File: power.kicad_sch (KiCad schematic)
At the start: 21 parts, among them J2 Conn_01x09_Pin, Q2 IRF840A, SW2 DOWNLOAD, U2 UC3843_DIP8, U7 AP2112K-3.3, U8 ESP32-S3-MINI-1

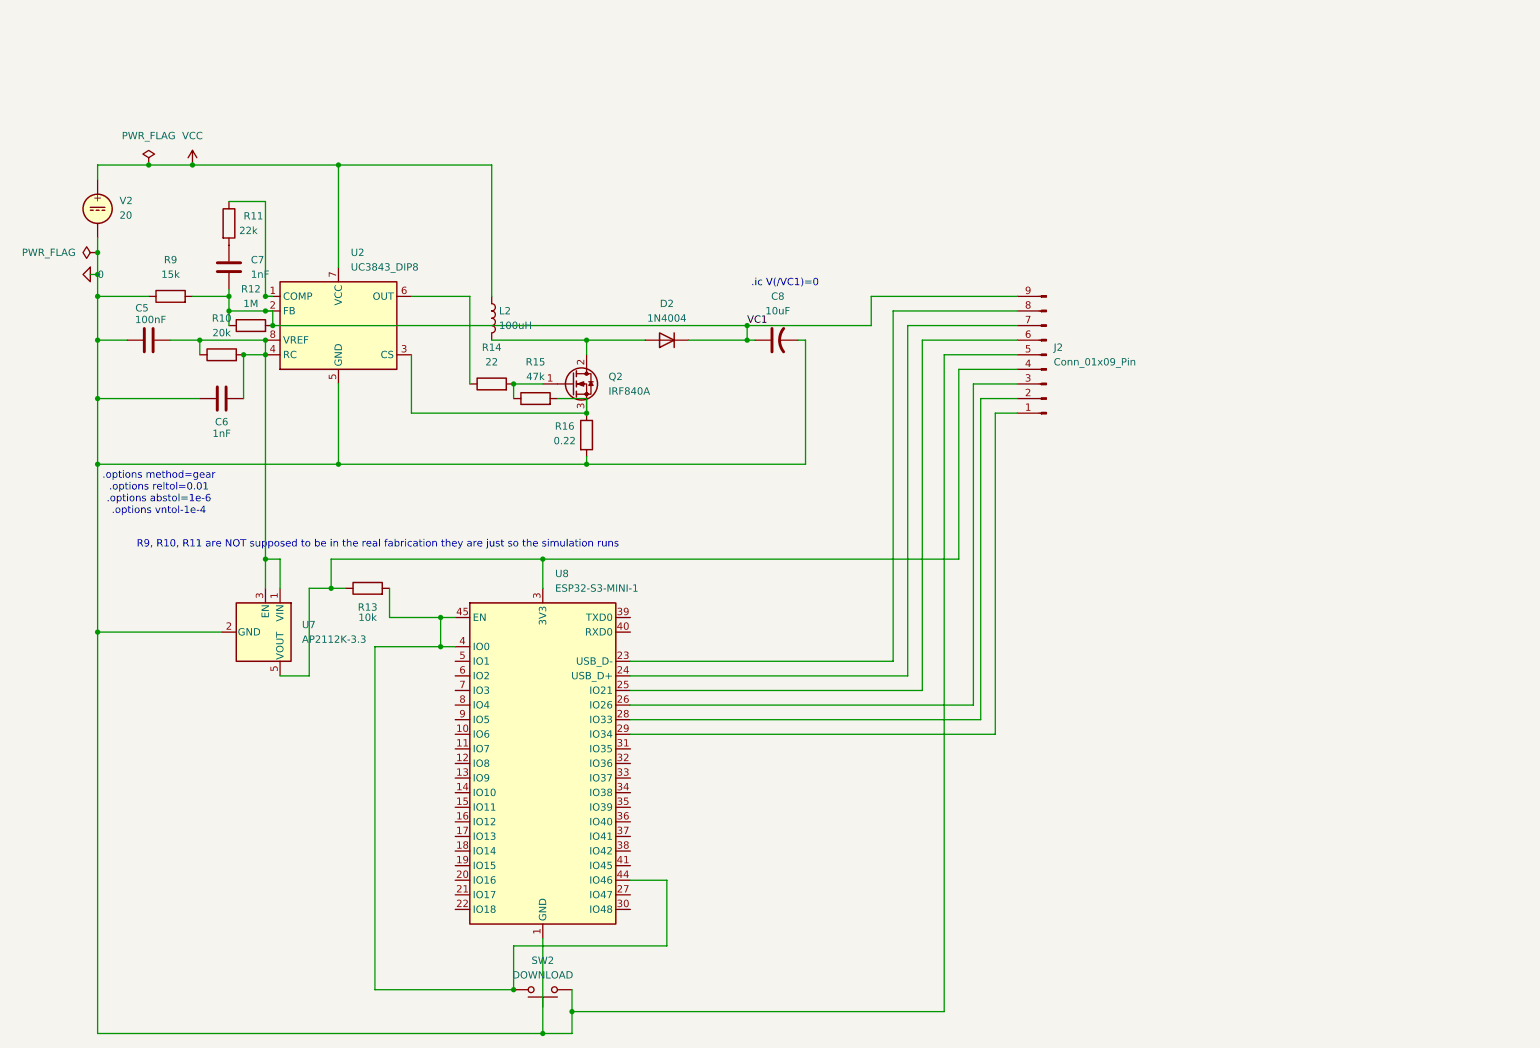
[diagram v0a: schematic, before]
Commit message: improve boost converter design and move to net labels
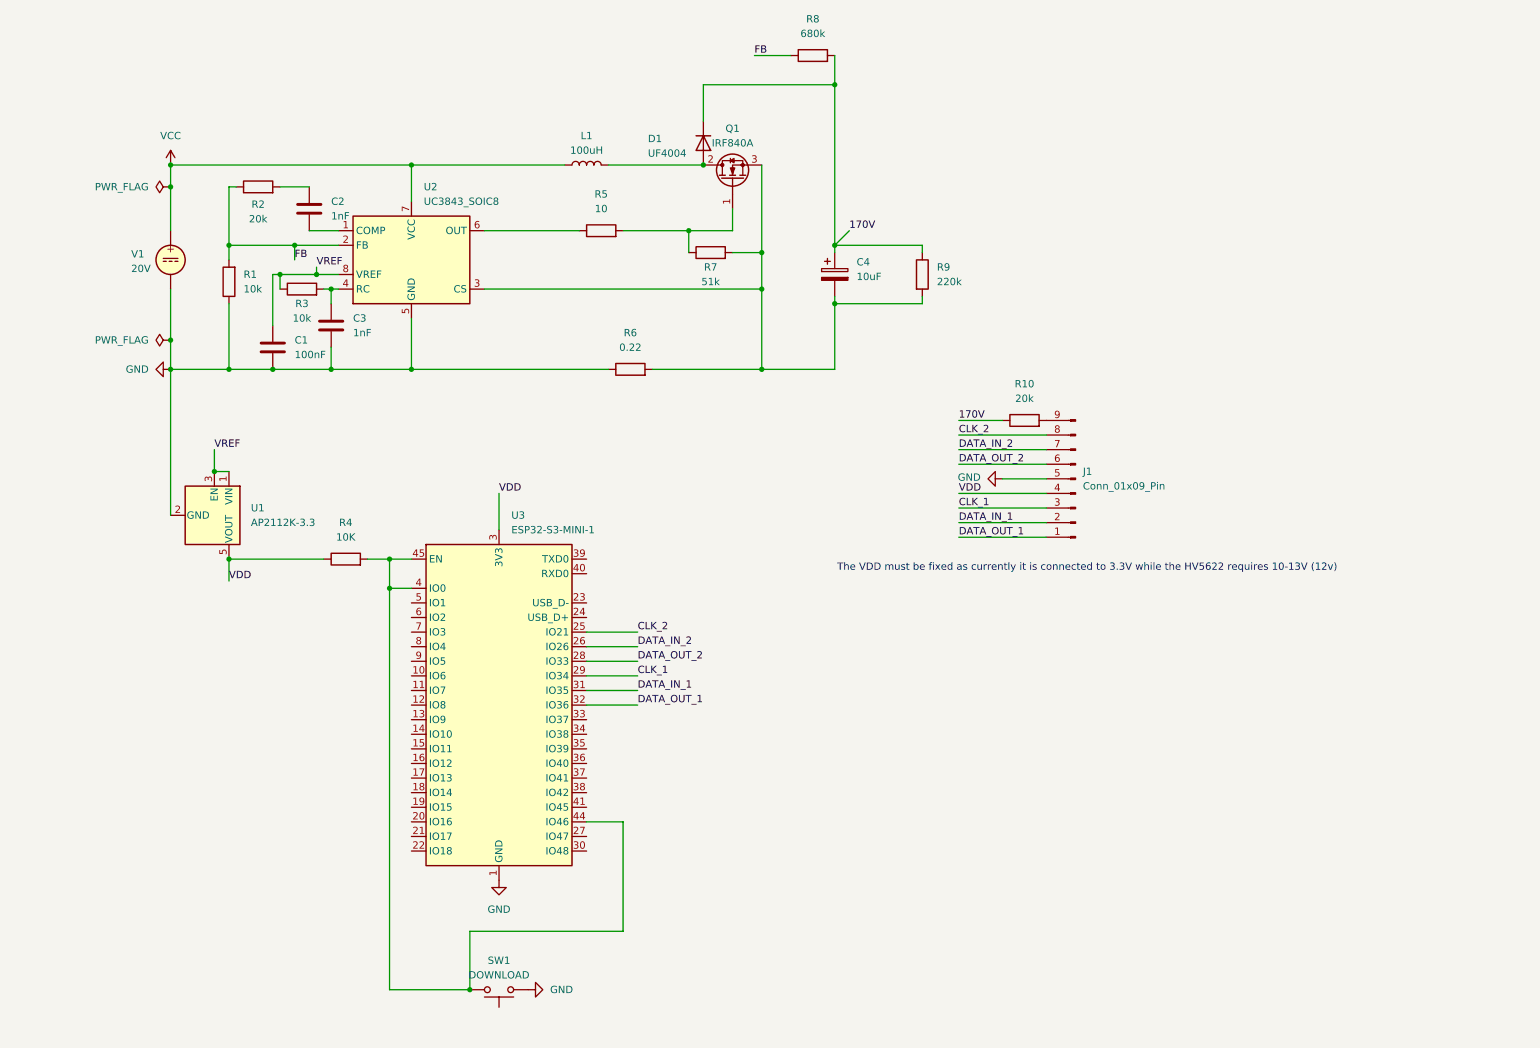
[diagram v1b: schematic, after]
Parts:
- removed C5: 100nF, Capacitor_SMD:C_0402_1005Metric, symbol Device:C
- removed C6, C7: 1nF, Capacitor_SMD:C_0402_1005Metric, symbol Device:C
- removed C8: 10uF, Capacitor_SMD:CP_Elec_10x12.5, symbol Device:C_US
- removed D2: 1N4004, Diode_THT:D_DO-41_SOD81_P10.16mm_Horizontal, symbol Diode:1N4004
- removed J2: Conn_01x09_Pin, symbol Connector:Conn_01x09_Pin
- removed L2: 100uH, Inductor_SMD:L_TaiTech_TMPC1265_13.5x12.5mm, symbol Device:L
- removed Q2: IRF840A, Package_TO_SOT_THT:TO-220-3_Vertical, symbol Transistor_FET:IRF840A
- removed R11: 22k, Resistor_SMD:R_1210_3225Metric, symbol Device:R
- removed R12: 1M, Resistor_SMD:R_1210_3225Metric, symbol Device:R
- removed R13: 10k, Resistor_SMD:R_1210_3225Metric, symbol Device:R
- removed R14: 22, Resistor_SMD:R_1210_3225Metric, symbol Device:R
- removed R15: 47k, Resistor_SMD:R_1210_3225Metric, symbol Device:R
- removed R16: 0.22, Resistor_SMD:R_2512_6332Metric, symbol Device:R
- removed SW2: DOWNLOAD, Button_Switch_SMD:SW_Push_1P1T_NO_CK_KSC6xxJ, symbol Switch:SW_Push
- removed U7: AP2112K-3.3, Package_TO_SOT_SMD:SOT-23-5, symbol Regulator_Linear:AP2112K-3.3
- removed U8: ESP32-S3-MINI-1, RF_Module:ESP32-S2-MINI-1, symbol RF_Module:ESP32-S3-MINI-1
- removed V2: 20, symbol Simulation_SPICE:VDC
- added C1: 100nF, Capacitor_SMD:C_01005_0402Metric, symbol Device:C
- added C2, C3: 1nF, Capacitor_SMD:C_01005_0402Metric, symbol Device:C
- added C4: 10uF, Capacitor_SMD:CP_Elec_4x3, symbol Device:C_Polarized
- added D1: UF4004, Diode_THT:D_DO-201AD_P15.24mm_Horizontal, symbol Diode:UF5404
- added J1: Conn_01x09_Pin, symbol Connector:Conn_01x09_Pin
- added L1: 100uH, Inductor_SMD:L_6.3x6.3_H3, symbol Device:L
- added Q1: IRF840A, Package_TO_SOT_THT:TO-220-3_Vertical, symbol Transistor_FET:IRF840A
- added R1, R3: 10k, Resistor_SMD:R_0201_0603Metric, symbol Device:R
- added R2: 20k, Resistor_SMD:R_0201_0603Metric, symbol Device:R
- added R4: 10K, symbol Device:R
- added R5: 10, Resistor_SMD:R_0201_0603Metric, symbol Device:R
- added R6: 0.22, Resistor_SMD:R_0201_0603Metric, symbol Device:R
- added R7: 51k, Resistor_SMD:R_0201_0603Metric, symbol Device:R
- added R8: 680k, Resistor_SMD:R_0201_0603Metric, symbol Device:R
- added SW1: DOWNLOAD, Button_Switch_SMD:SW_Push_1P1T_NO_CK_KSC6xxJ, symbol Switch:SW_Push
- added U1: AP2112K-3.3, Package_TO_SOT_SMD:SOT-23-5, symbol Regulator_Linear:AP2112K-3.3
- added U3: ESP32-S3-MINI-1, RF_Module:ESP32-S2-MINI-1, symbol RF_Module:ESP32-S3-MINI-1
- added V1: 20V, symbol Simulation_SPICE:VDC
- R10: footprint Resistor_SMD:R_1210_3225Metric -> (none)
- R9: value 15k -> 220k; footprint Resistor_SMD:R_1210_3225Metric -> Resistor_SMD:R_0201_0603Metric
- U2: value UC3843_DIP8 -> UC3843_SOIC8; footprint Package_DIP:DIP-8_W7.62mm -> Package_SO:SOIC-8_3.9x4.9mm_P1.27mm
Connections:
- net VCC: now also L1.1, V1.1
- net at U2.1 (COMP): now also C2.1
- net at U2.3 (CS): now also R9.2, C4.2, Q1.3 (S), R6.2, R7.2
- net at U2.6 (OUT): now also R5.1
- net 0 renamed 170V
- net 170V: now also R10.1, C4.1, D1.1 (K), R8.2; no longer U2.5 (GND)
- net VC1 renamed FB
- net FB: now also R1.2, R2.1, R8.1; no longer R9.2
- new net: J1.9 (Pin_9), R10.2
- new net: R4.2, SW1.2, U3.4 (IO0), U3.44 (IO46), U3.45 (EN)
- new net: Q1.1 (G), R5.2, R7.1
- new net: C3.1, R3.2, U2.4 (RC)
- new net: C2.2, R2.2
- new net: D1.2 (A), L1.2, Q1.2 (D)
- new net CLK_1: J1.3 (Pin_3), U3.29 (IO34)
- new net CLK_2: J1.8 (Pin_8), U3.25 (IO21)
- new net DATA_IN_1: J1.2 (Pin_2), U3.31 (IO35)
- new net DATA_IN_2: J1.7 (Pin_7), U3.26 (IO26)
- new net DATA_OUT_1: J1.1 (Pin_1), U3.32 (IO36)
- new net DATA_OUT_2: J1.6 (Pin_6), U3.28 (IO33)
- new net GND: C1.2, C3.2, J1.5 (Pin_5), R1.1, R6.1, SW1.1, U1.2 (GND), U2.5 (GND), U3.1 (GND), U3.2 (GND), U3.42 (GND), U3.43 (GND), U3.46 (GND), U3.47 (GND), U3.48 (GND), U3.49 (GND), U3.50 (GND), U3.51 (GND), U3.52 (GND), U3.53 (GND), U3.54 (GND), U3.55 (GND), U3.56 (GND), U3.57 (GND), U3.58 (GND), U3.59 (GND), U3.60 (GND), U3.61 (GND), U3.62 (GND), U3.63 (GND), U3.64 (GND), U3.65 (GND), V1.2
- new net VDD: J1.4 (Pin_4), R4.1, U1.5 (VOUT), U3.3 (3V3)
- new net VREF: C1.1, R3.1, U1.1 (VIN), U1.3 (EN), U2.8 (VREF)
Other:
- note added: "The VDD must be fixed as currently it is connected to 3.3V while the HV5622 requires 10-13V (12v)"
- note removed: ".ic V(/VC1)=0"
- note removed: ".options method=gear .options reltol=0.01 .options abstol=1e-6 .options vntol-1e-4"
- note removed: "R9, R10, R11 are NOT supposed to be in the real fabrication they are just so the simulation runs"

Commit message: add usb c pd deceiver footprint
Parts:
- J1: footprint (none) -> Connector_PinSocket_2.54mm:PinSocket_1x09_P2.54mm_Vertical
- R10, R4: footprint (none) -> Resistor_SMD:R_0201_0603Metric
- V1: footprint (none) -> USB_PD_Connector:USB C PD Deceiver
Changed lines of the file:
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@@
 			)
 		)
-		(property "Footprint" ""
+		(property "Footprint" "Resistor_SMD:R_0201_0603Metric"
 			(at 180.34 91.948 90)
 			(hide yes)
@@
 			)
 		)
-		(property "Footprint" ""
+		(property "Footprint" "USB_PD_Connector:USB C PD Deceiver"
 			(at 31.75 62.23 0)
 			(hide yes)
@@
 			)
 		)
-		(property "Footprint" ""
+		(property "Footprint" "Connector_PinSocket_2.54mm:PinSocket_1x09_P2.54mm_Vertical"
 			(at 189.23 100.33 0)
 			(hide yes)
@@
 			)
 		)
-		(property "Footprint" ""
+		(property "Footprint" "Resistor_SMD:R_0201_0603Metric"
 			(at 62.23 116.078 90)
 			(hide yes)

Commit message: ywah
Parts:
- removed R4: 10K, Resistor_SMD:R_0201_0603Metric, symbol Device:R
- removed SW1: DOWNLOAD, Button_Switch_SMD:SW_Push_1P1T_NO_CK_KSC6xxJ, symbol Switch:SW_Push
- removed U1: AP2112K-3.3, Package_TO_SOT_SMD:SOT-23-5, symbol Regulator_Linear:AP2112K-3.3
- removed U3: ESP32-S3-MINI-1, RF_Module:ESP32-S2-MINI-1, symbol RF_Module:ESP32-S3-MINI-1
- added H2, H3, H4, H5: MountingHole_Pad, MountingHole:MountingHole_2.2mm_M2_Pad, symbol Mechanical:MountingHole_Pad
- added R11: 68k, symbol Device:R
- C1: footprint Capacitor_SMD:C_01005_0402Metric -> Capacitor_THT:C_Disc_D5.0mm_W2.5mm_P2.50mm; LCSC Part # (none) -> C710459
- C2, C3: footprint Capacitor_SMD:C_01005_0402Metric -> Capacitor_THT:C_Disc_D5.0mm_W2.5mm_P2.50mm; LCSC Part # (none) -> C49326697
- C4: footprint Capacitor_SMD:CP_Elec_4x3 -> Capacitor_THT:C_Radial_D10.0mm_H12.5mm_P5.00mm; LCSC Part # (none) -> C231218
- D1: footprint Diode_THT:D_DO-201AD_P15.24mm_Horizontal -> Diode_THT:D_DO-41_SOD81_P10.16mm_Horizontal; LCSC Part # (none) -> C5455815
- L1: footprint Inductor_SMD:L_6.3x6.3_H3 -> Inductor_THT:L_Toroid_Vertical_L13.0mm_W6.5mm_P5.60mm; LCSC Part # (none) -> C5273830
- R1, R3: footprint Resistor_SMD:R_0201_0603Metric -> Resistor_THT:R_Axial_DIN0207_L6.3mm_D2.5mm_P7.62mm_Horizontal; LCSC Part # (none) -> C1489
- R10, R2: footprint Resistor_SMD:R_0201_0603Metric -> Resistor_THT:R_Axial_DIN0207_L6.3mm_D2.5mm_P7.62mm_Horizontal; LCSC Part # (none) -> C102303
- R5: footprint Resistor_SMD:R_0201_0603Metric -> Resistor_THT:R_Axial_DIN0207_L6.3mm_D2.5mm_P7.62mm_Horizontal; LCSC Part # (none) -> C49652945; now left out of the parts list
- R6: footprint Resistor_SMD:R_0201_0603Metric -> Resistor_THT:R_Axial_DIN0516_L15.5mm_D5.0mm_P20.32mm_Horizontal; LCSC Part # (none) -> C176084
- R7: footprint Resistor_SMD:R_0201_0603Metric -> Resistor_THT:R_Axial_DIN0207_L6.3mm_D2.5mm_P7.62mm_Horizontal; LCSC Part # (none) -> C52209904
- R8: footprint Resistor_SMD:R_0201_0603Metric -> Resistor_THT:R_Axial_DIN0207_L6.3mm_D2.5mm_P7.62mm_Horizontal; LCSC Part # (none) -> C53069497
- R9: footprint Resistor_SMD:R_0201_0603Metric -> Resistor_THT:R_Axial_DIN0207_L6.3mm_D2.5mm_P7.62mm_Horizontal; LCSC Part # (none) -> C352118
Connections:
- net 170V: now also R11.1
- net GND: now also H2.1, H3.1, H4.1, H5.1
- net at C4.2, Q1.3 (S), R6.2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: now also R11.2
- net VCC renamed 20V
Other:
- added sheet Breakout (breakout.kicad_sch)
- added sheet Logic (logic.kicad_sch)
- note added: ".options method=gear .options reltol=0.01 .options abstol=1e-6 .options vntol=1e-4"
